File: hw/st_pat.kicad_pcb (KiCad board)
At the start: 2 copper layers, 18 parts, among them J4 BATTERY, SW1 SW_PWR, SW2 BTN_RST, SW3 BTN, SW4 BTN, SW5 BTN, U1 FGPMMOPA6H, U2 FEATHER_M0_BASIC_PROTO, U3 LIS2MDL_ADAFRUIT, U4 Sharp_Display

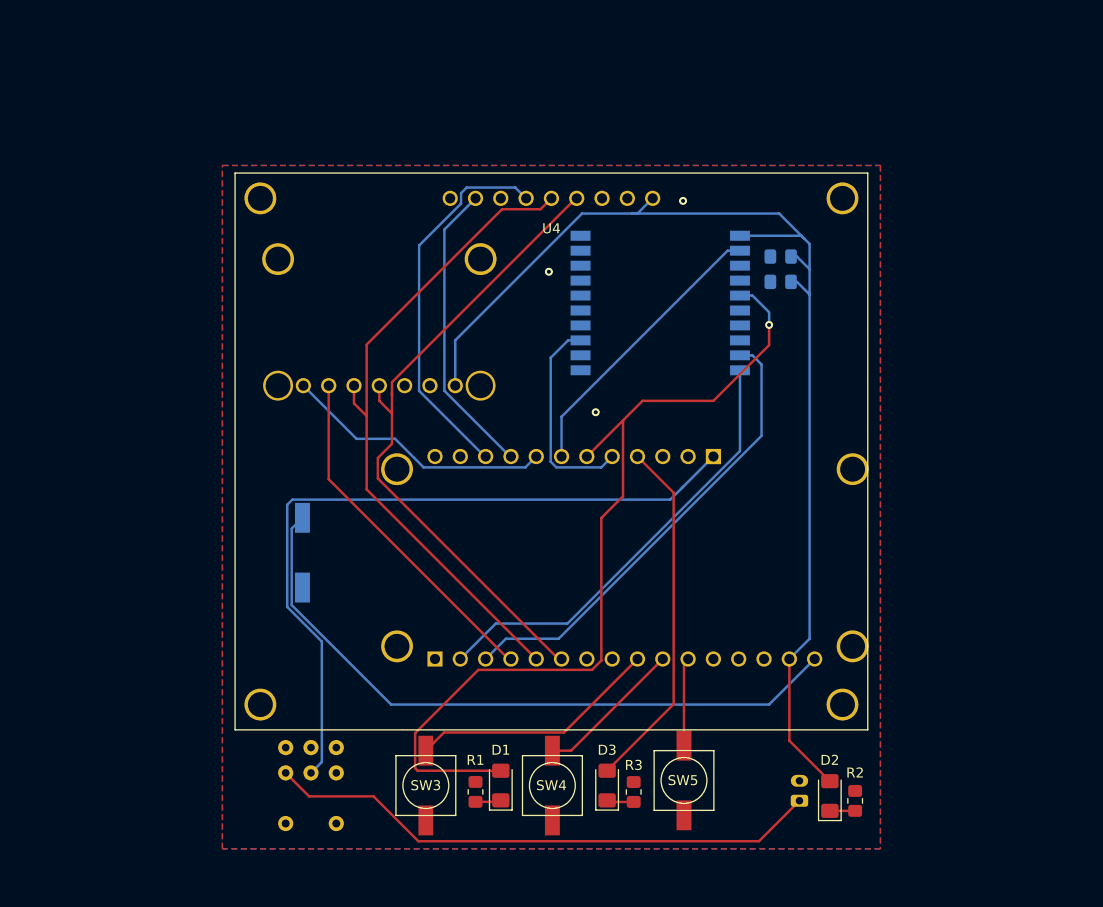
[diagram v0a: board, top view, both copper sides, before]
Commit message: Add missing telemetry breakout board
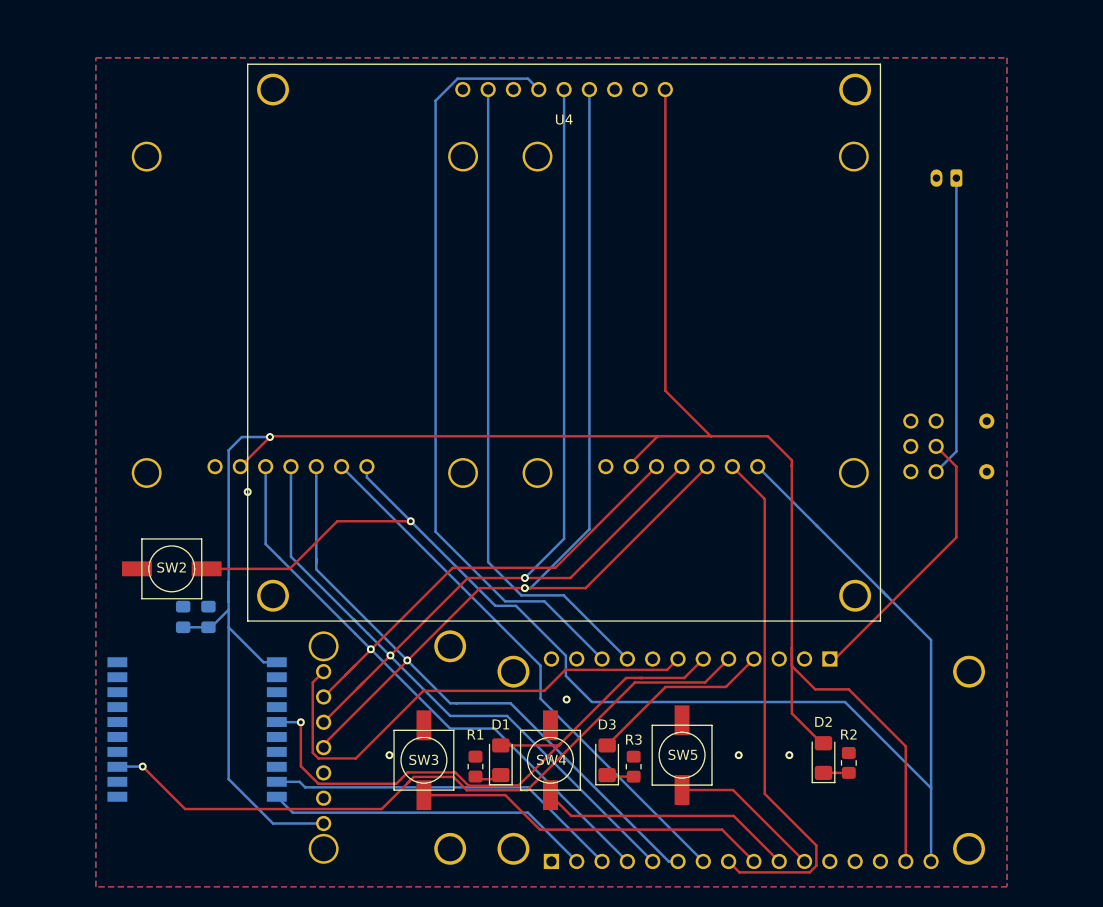
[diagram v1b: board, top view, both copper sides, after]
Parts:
- added U5: Telemetry_Breakout, st_pat:Telemetry_Breakout, B.Cu at (175.1, 67.7)
- added U6: Telemetry_Breakout, st_pat:Telemetry_Breakout, B.Cu at (135.9, 67.7)
- SW2: moved to F.Cu
- moved C1 68.7 mm to (102.7, 97.4), turned to 90 degrees
- moved C2 67.9 mm to (105.3, 97.4), turned to 90 degrees
- moved SW1 66.3 mm to (175.8, 77.7), turned to 270 degrees
- moved J4 64.4 mm to (180.3, 53.3), turned to 180 degrees
- moved U1 63.2 mm to (104.1, 98.4)
- moved U3 59.6 mm to (134.6, 115.6), turned to 90 degrees
- moved U2 23.4 mm to (158.8, 111.8)
- moved SW2 13.3 mm to (101.6, 92.5), turned to 180 degrees
- moved U4 11.0 mm to (151.1, 44.5)
- moved R2 3.86 mm to (169.5, 112.0)
- moved D2 3.86 mm to (167.0, 111.5)
- moved R1 2.54 mm to (132.1, 112.4)
- moved SW5 2.54 mm to (152.9, 111.3), turned to 90 degrees
- moved D1 2.54 mm to (134.6, 111.8)
- moved D3 2.54 mm to (145.3, 111.8)
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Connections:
- U1 pad 2: /GPS_RST_D10 -> (no net)
- U2 pad P1_7: (no net) -> /SRAD_RECV_CS_A5
- U2 pad P1_8: (no net) -> /COTS_RECV_CS_A4
- U2 pad P2_7: /GPS_RST_D10 -> /CPS_CS_D10
- U2 pad P2_8: /CPS_CS_D9 -> (no net)
- U3 pad 7: /CPS_CS_D9 -> /CPS_CS_D10
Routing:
- net +3V3: track 118.1 -> 220.0 mm, vias 0 -> 1
- net /SCK: track 66.4 -> 163.1 mm, vias 0 -> 2
- net /MOSI: track 66.8 -> 156.4 mm, vias 0 -> 2
- net /RST: track 67.7 -> 142.3 mm, vias 0 -> 1
- net /MISO: track 35.2 -> 101.6 mm, vias 0 -> 1
- net /SRAD_RECV_CS_A5: track 0.00 -> 54.7 mm
- net /COTS_RECV_CS_A4: track 0.00 -> 53.1 mm
- net /GPS_PPS_D12: track 21.0 -> 70.9 mm, vias 0 -> 1
- net /CPS_CS_D10: track 0.00 -> 49.6 mm
- net +BATT: track 73.8 -> 27.7 mm
- net /SHARP_CS_D5: track 38.2 -> 77.0 mm
- net /SHARP_DISP_D6: track 30.0 -> 65.4 mm
- net /GPS_RST_D10: track 28.8 -> 0.00 mm
- net /GPS_FIX_D11: track 89.3 -> 60.6 mm
- net /CPS_CS_D9: track 27.2 -> 0.00 mm
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
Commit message: Rearrange board layout
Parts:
- added  : , MountingHole:MountingHole_2.5mm_Pad, F.Cu at (97.0, 121.4)
- added  : , MountingHole:MountingHole_2.5mm_Pad, F.Cu at (97.0, 44.2)
- added  : , MountingHole:MountingHole_2.5mm_Pad, F.Cu at (182.4, 44.2)
- moved J4 79.4 mm to (101.1, 49.3), turned to 270 degrees
- moved U6 26.6 mm to (113.8, 52.8), turned to 180 degrees
- moved U5 21.9 mm to (165.6, 87.4), turned to 0 degrees
- moved SW1 13.2 mm to (176.3, 90.9)
- moved SW3 2.54 mm to (124.5, 111.8)
- moved SW5 2.09 mm to (154.9, 111.8)
- moved D1 1.27 mm to (133.3, 111.8)
- moved R1 1.27 mm to (130.8, 112.4)
- moved U4 1.27 mm to (149.9, 44.5)
- moved D3 0.63 mm to (145.9, 111.8)
- moved R3 0.63 mm to (148.6, 112.4)
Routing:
- net Net-(J4-Pad1): track 30.8 -> 114.2 mm
- net /RST: track 142.3 -> 168.6 mm
- net /SHARP_CS_D5: track 77.0 -> 60.3 mm
- net +BATT: track 27.7 -> 15.5 mm
- net +3V3: track 220.0 -> 231.4 mm
- net /MISO: track 101.6 -> 110.8 mm
- net /GPS_FIX_D11: track 60.6 -> 69.7 mm
- net /SRAD_RECV_CS_A5: track 54.7 -> 62.8 mm, vias 0 -> 1
- net /MOSI: track 156.4 -> 150.7 mm
- net /SCK: track 163.1 -> 160.2 mm
- net /BTN_A3: track 35.9 -> 38.7 mm
- net /COTS_RECV_CS_A4: track 53.1 -> 55.9 mm
- net /BTN_A1: track 15.5 -> 13.0 mm
- net /SHARP_DISP_D6: track 65.4 -> 66.8 mm
- net /GPS_PPS_D12: track 70.9 -> 70.1 mm
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
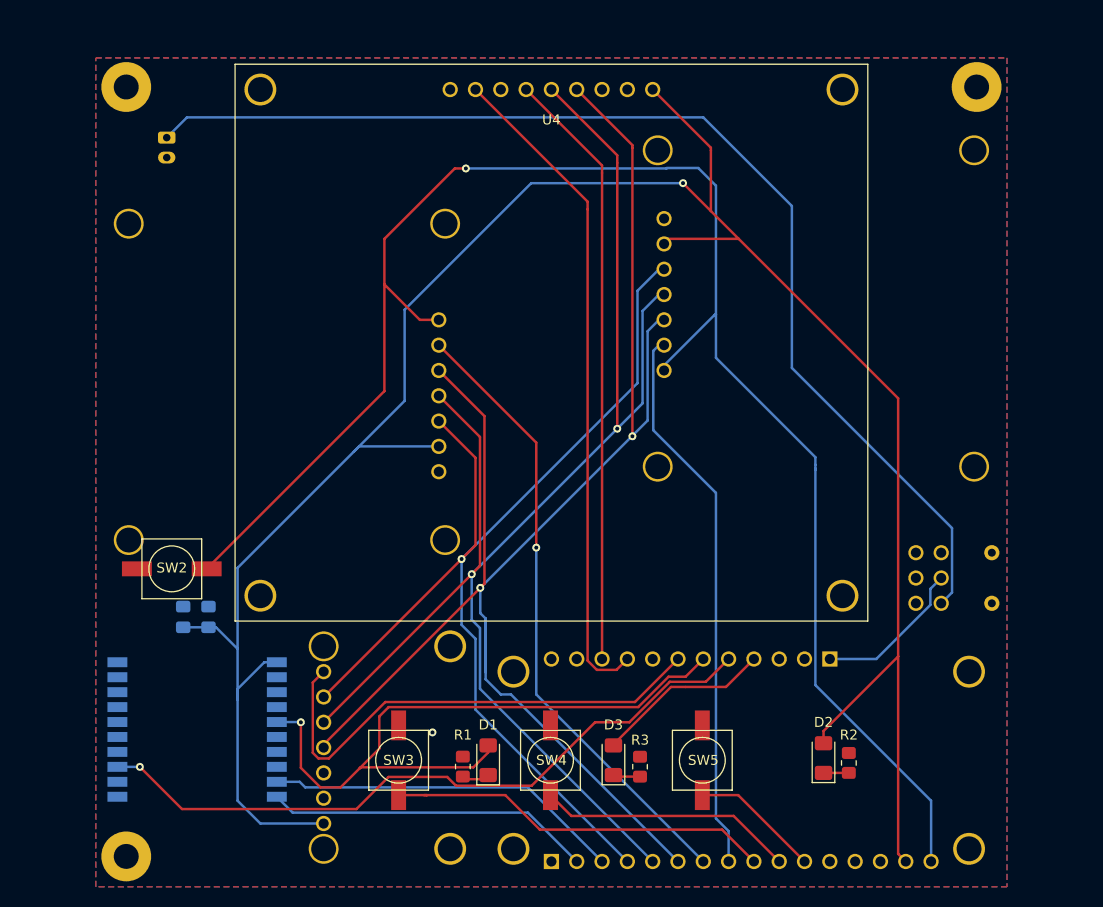
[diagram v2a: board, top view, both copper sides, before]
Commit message: Redo layout and fix some small schematic issues
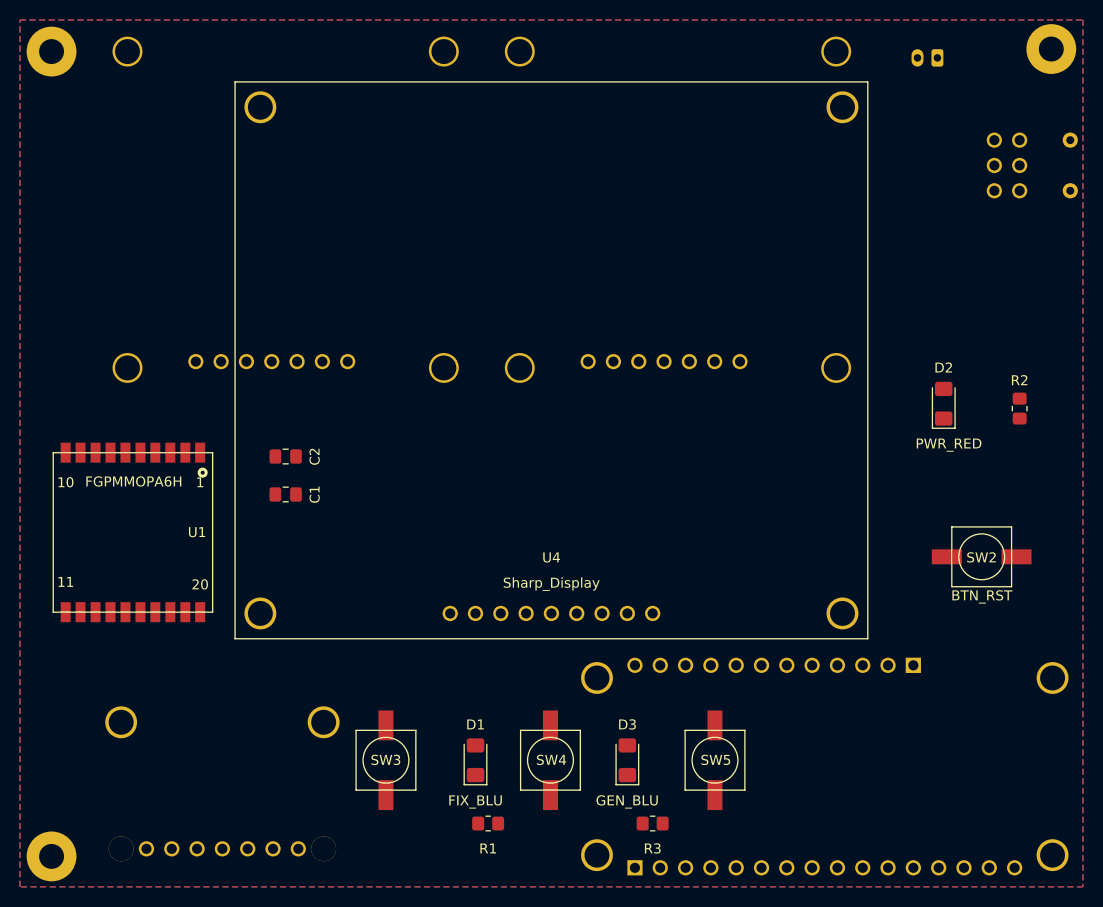
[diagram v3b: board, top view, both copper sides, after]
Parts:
- C1, C2, U1: moved to F.Cu
- moved SW2 81.3 mm to (182.9, 91.4), turned to 0 degrees
- moved J4 77.8 mm to (178.4, 41.3), turned to 180 degrees
- moved U4 56.4 mm to (129.5, 97.0), turned to 180 degrees
- moved SW1 42.1 mm to (184.2, 49.5)
- moved R2 39.5 mm to (186.7, 76.5)
- moved D2 37.6 mm to (179.1, 76.0)
- moved U5 31.2 mm to (173.4, 57.1), turned to 90 degrees
- moved U3 26.2 mm to (111.8, 102.9), turned to 180 degrees
- moved U6 20.6 mm to (134.0, 57.1), turned to 90 degrees
- moved C2 17.9 mm to (113.0, 81.3), turned to 0 degrees
- moved C1 16.0 mm to (113.0, 85.1), turned to 0 degrees
- moved U1 10.3 mm to (108.0, 88.9), turned to 270 degrees
- moved U2 8.41 mm to (167.1, 112.4)
- moved   8.41 mm to (189.9, 40.4)
- moved   8.29 mm to (89.5, 40.6)
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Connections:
- net /RX renamed /GPS_TX
- net /TX renamed /GPS_RX
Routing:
- net +3V3: track 231.4 -> 0.00 mm, vias 1 -> 0
- net /RST: track 168.6 -> 0.00 mm, vias 1 -> 0
- net /SCK: track 160.2 -> 0.00 mm, vias 2 -> 0
- net /MOSI: track 150.7 -> 0.00 mm, vias 2 -> 0
- net Net-(J4-Pad1): track 114.2 -> 0.00 mm
- net /MISO: track 110.8 -> 0.00 mm, vias 1 -> 0
- net /GPS_PPS_D12: track 70.1 -> 0.00 mm, vias 1 -> 0
- net /GPS_FIX_D11: track 69.7 -> 0.00 mm, vias 1 -> 0
- net /SHARP_DISP_D6: track 66.8 -> 0.00 mm
- net /SRAD_RECV_CS_A5: track 62.8 -> 0.00 mm, vias 1 -> 0
- net /SHARP_CS_D5: track 60.3 -> 0.00 mm
- net /COTS_RECV_CS_A4: track 55.9 -> 0.00 mm
- net /CPS_CS_D10: track 49.6 -> 0.00 mm
- net /BTN_A3: track 38.7 -> 0.00 mm
- net /GPS_TX: track 36.0 -> 0.00 mm
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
